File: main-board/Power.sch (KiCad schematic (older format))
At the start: 63 parts, among them J4 5V Input, Q1 N Channel, Q10 N Channel, Q11 N Channel, Q12 N Channel, Q13 P Channel, Q14 P Channel, Q15 P Channel, Q16 P Channel, Q17 P Channel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

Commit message: Swap power filter caps, tighten up trace routing
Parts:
- C47: footprint Capacitors_SMD:CP_Elec_5x4.5 -> Capacitors_SMD:CP_Elec_4x4.5
- C48: footprint Capacitors_SMD:CP_Elec_4x4.5 -> Capacitors_SMD:CP_Elec_5x5.3
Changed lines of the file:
@@
 F 0 "C47" H 1341 1596 50  0000 L CNN
 F 1 "10uF" H 1341 1505 50  0000 L CNN
-F 2 "Capacitors_SMD:CP_Elec_5x4.5" H 1250 1550 50  0001 C CNN
+F 2 "Capacitors_SMD:CP_Elec_4x4.5" H 1250 1550 50  0001 C CNN
 F 3 "~" H 1250 1550 50  0001 C CNN
 	1    1250 1550
@@
 F 0 "C48" H 2391 1596 50  0000 L CNN
 F 1 "22uF" H 2391 1505 50  0000 L CNN
-F 2 "Capacitors_SMD:CP_Elec_4x4.5" H 2300 1550 50  0001 C CNN
+F 2 "Capacitors_SMD:CP_Elec_5x5.3" H 2300 1550 50  0001 C CNN
 F 3 "~" H 2300 1550 50  0001 C CNN
 	1    2300 1550

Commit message: GPIO control lines for the MOSFET array
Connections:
- net PWR1_Control renamed PWR1_CTRL
- net PWR2_Control renamed PWR2_CTRL
- net PWR3_Control renamed PWR3_CTRL
- net PWR4_Control renamed PWR4_CTRL
- net PWR5_Control renamed PWR5_CTRL
- net PWR6_Control renamed PWR6_CTRL
- net PWR7_Control renamed PWR7_CTRL
- net PWR8_Control renamed PWR8_CTRL
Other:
- moved on the sheet: C54, C55, C56, C57, FB10, FB12, FB14, FB16, Q10, Q11, Q12, Q13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

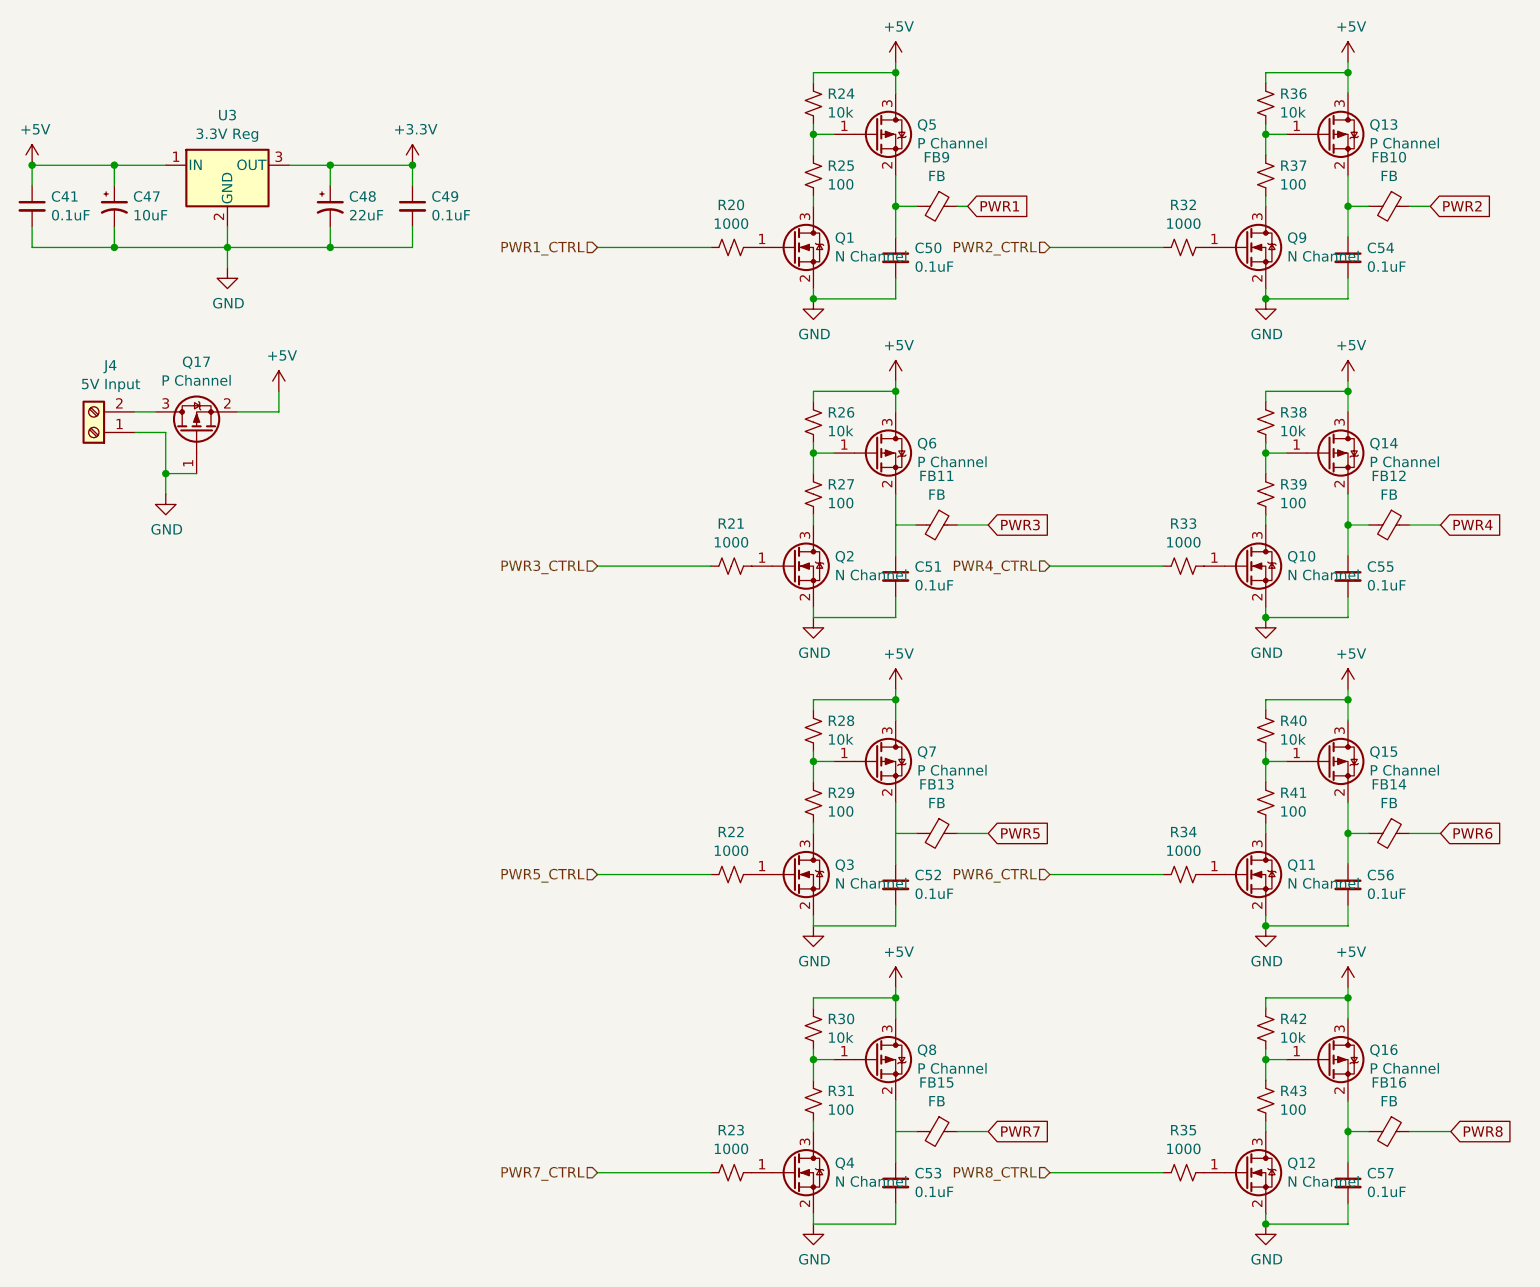
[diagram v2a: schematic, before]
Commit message: Had the p-channel FETs in the wrong orientation, and an unnecessary resistor.
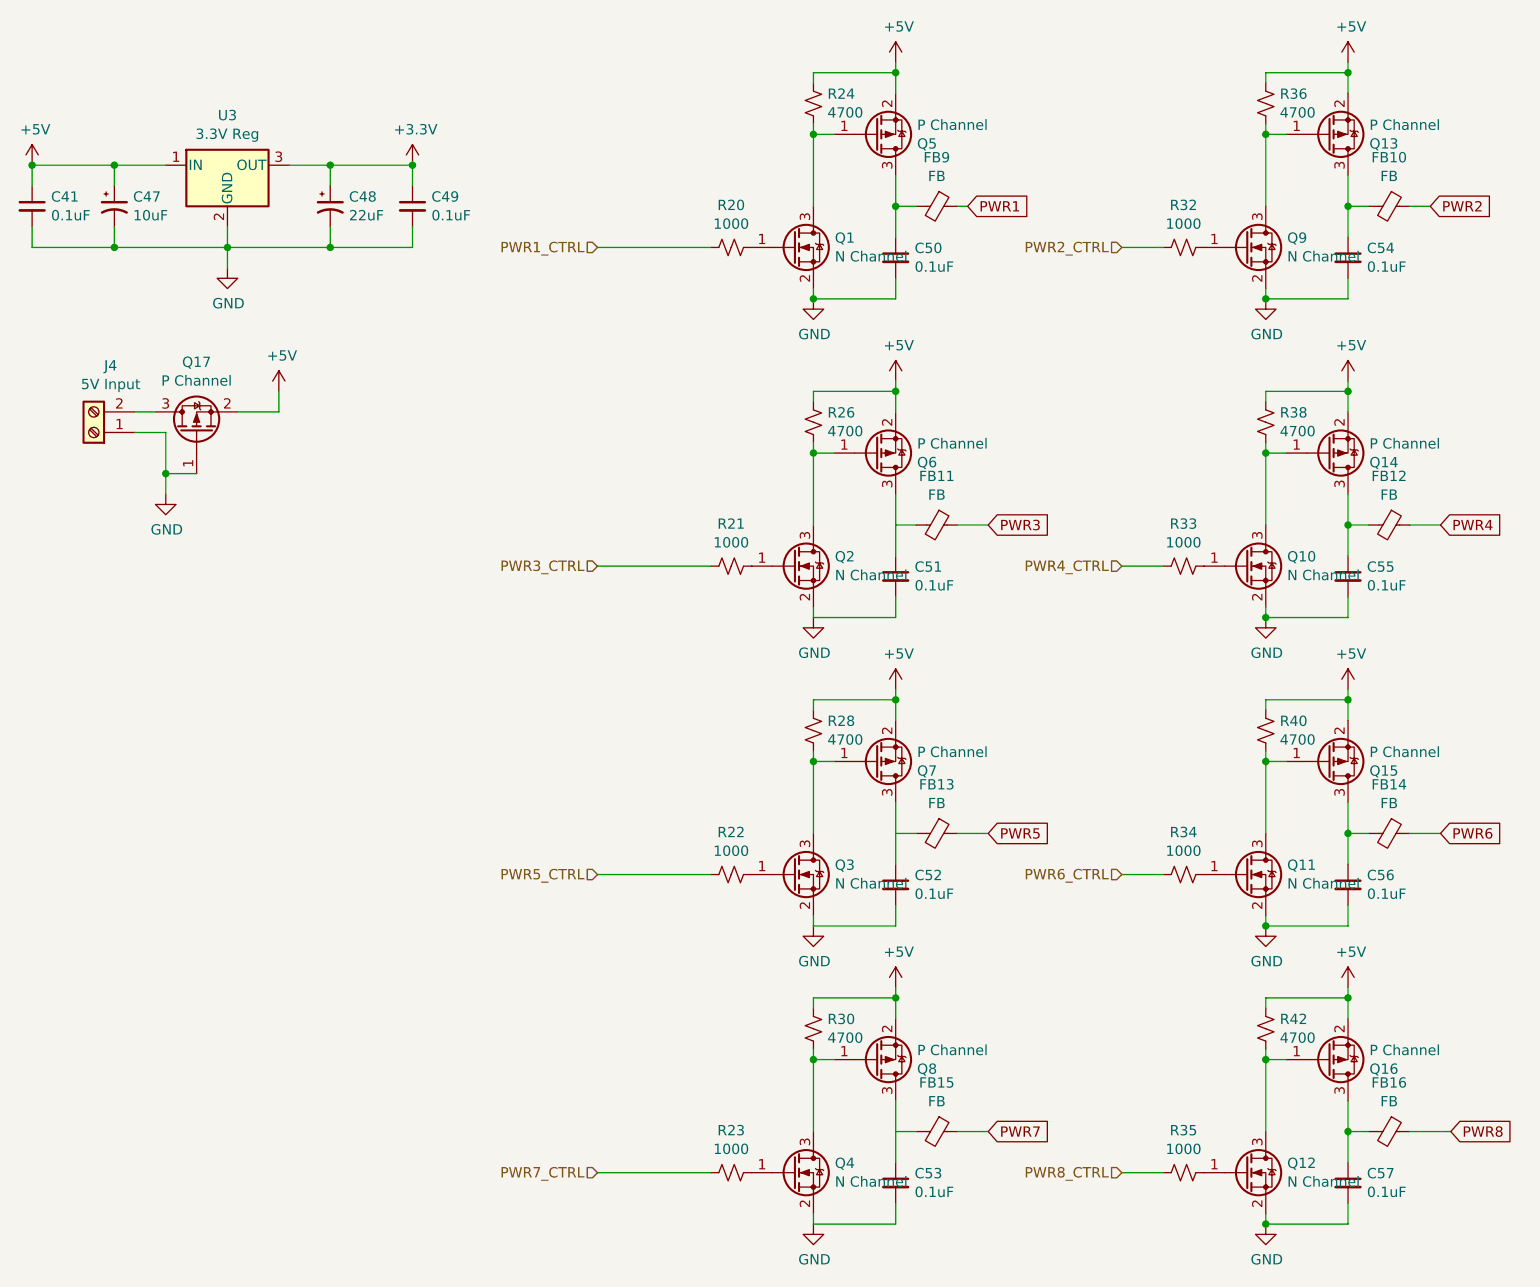
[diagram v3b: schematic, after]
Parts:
- removed R25, R27, R29, R31, R37, R39, R41, R43: 100, Resistors_SMD:R_0805, symbol Device:R_Small_US
- R24, R26, R28, R30, R36, R38, R40, R42: value 10k -> 4700
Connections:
- net +5V: now also Q13.2 (S), Q14.2 (S), Q15.2 (S), Q16.2 (S), Q5.2 (S), Q6.2 (S), Q7.2 (S), Q8.2 (S); no longer Q13.3 (D), Q14.3 (D), Q15.3 (D), Q16.3 (D), Q5.3 (D), Q6.3 (D), Q7.3 (D), Q8.3 (D)
- net at C50.1, FB9.2: now also Q5.3 (D); no longer Q5.2 (S)
- net at C57.1, FB16.2: now also Q16.3 (D); no longer Q16.2 (S)
- net at C53.1, FB15.2: now also Q8.3 (D); no longer Q8.2 (S)
- net at C52.1, FB13.2: now also Q7.3 (D); no longer Q7.2 (S)
- net at C56.1, FB14.2: now also Q15.3 (D); no longer Q15.2 (S)
- net at C51.1, FB11.2: now also Q6.3 (D); no longer Q6.2 (S)
- net at C55.1, FB12.2: now also Q14.3 (D); no longer Q14.2 (S)
- net at C54.1, FB10.2: now also Q13.3 (D); no longer Q13.2 (S)
- net at Q5.1 (G), R24.2: now also Q1.3 (D)
- net at Q13.1 (G), R36.2: now also Q9.3 (D)
- net at Q6.1 (G), R26.2: now also Q2.3 (D)
- net at Q14.1 (G), R38.2: now also Q10.3 (D)
- net at Q7.1 (G), R28.2: now also Q3.3 (D)
- net at Q15.1 (G), R40.2: now also Q11.3 (D)
- net at Q8.1 (G), R30.2: now also Q4.3 (D)
- net at Q16.1 (G), R42.2: now also Q12.3 (D)
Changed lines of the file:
@@
 P 4650 1050
 F 0 "R24" H 4718 1096 50  0000 L CNN
-F 1 "10k" H 4718 1005 50  0000 L CNN
+F 1 "4700" H 4718 1005 50  0000 L CNN
 F 2 "Resistors_SMD:R_0805" H 4650 1050 50  0001 C CNN
 F 3 "~" H 4650 1050 50  0001 C CNN
@@
 	4650 1200 4750 1200
 Connection ~ 4650 1200
-Wire Wire Line
-	4650 1300 4650 1200
-$Comp
-L Device:R_Small_US R25
-U 1 1 611CCFA1
-P 4650 1400
-F 0 "R25" H 4718 1446 50  0000 L CNN
-F 1 "100" H 4718 1355 50  0000 L CNN
-F 2 "Resistors_SMD:R_0805" H 4650 1400 50  0001 C CNN
-F 3 "~" H 4650 1400 50  0001 C CNN
-	1    4650 1400
-	1    0    0    -1
-$EndComp
-Wire Wire Line
-	4650 1550 4650 1500
 Wire Wire Line
 	4650 1950 4650 2000
@@
 F 3 "~" H 4950 1200 50  0001 C CNN
 	1    4950 1200
-	1    0    0    -1
+	1    0    0    1
 $EndComp
 $Comp
@@
 P 6850 1050
 F 0 "R36" H 6918 1096 50  0000 L CNN
-F 1 "10k" H 6918 1005 50  0000 L CNN
+F 1 "4700" H 6918 1005 50  0000 L CNN
 F 2 "Resistors_SMD:R_0805" H 6850 1050 50  0001 C CNN
 F 3 "~" H 6850 1050 50  0001 C CNN
@@
 	6850 1200 6950 1200
 Connection ~ 6850 1200
-Wire Wire Line
-	6850 1300 6850 1200
-$Comp
-L Device:R_Small_US R37
-U 1 1 611DCBB1
-P 6850 1400
-F 0 "R37" H 6918 1446 50  0000 L CNN
-F 1 "100" H 6918 1355 50  0000 L CNN
-F 2 "Resistors_SMD:R_0805" H 6850 1400 50  0001 C CNN
-F 3 "~" H 6850 1400 50  0001 C CNN
-	1    6850 1400
-	1    0    0    -1
-$EndComp
-Wire Wire Line
-	6850 1550 6850 1500
 Wire Wire Line
 	6850 1950 6850 2000
@@
 $EndComp
 Wire Wire Line
-	6350 1750 5800 1750
+	6350 1750 6150 1750
 $Comp
 L Device:Q_NMOS_GSD Q9
@@
 F 3 "~" H 7150 1200 50  0001 C CNN
 	1    7150 1200
-	1    0    0    -1
+	1    0    0    1
 $EndComp
 $Comp
@@
 P 4650 2600
 F 0 "R26" H 4718 2646 50  0000 L CNN
-F 1 "10k" H 4718 2555 50  0000 L CNN
+F 1 "4700" H 4718 2555 50  0000 L CNN
 F 2 "Resistors_SMD:R_0805" H 4650 2600 50  0001 C CNN
 F 3 "~" H 4650 2600 50  0001 C CNN
@@
 	4650 2750 4750 2750
 Connection ~ 4650 2750
-Wire Wire Line
-	4650 2850 4650 2750
-$Comp
-L Device:R_Small_US R27
-U 1 1 611F4F2B
-P 4650 2950
-F 0 "R27" H 4718 2996 50  0000 L CNN
-F 1 "100" H 4718 2905 50  0000 L CNN
-F 2 "Resistors_SMD:R_0805" H 4650 2950 50  0001 C CNN
-F 3 "~" H 4650 2950 50  0001 C CNN
-	1    4650 2950
-	1    0    0    -1
-$EndComp
-Wire Wire Line
-	4650 3100 4650 3050
 Wire Wire Line
 	4650 3500 4650 3550
@@
 F 3 "~" H 4950 2750 50  0001 C CNN
 	1    4950 2750
-	1    0    0    -1
+	1    0    0    1
 $EndComp
 $Comp
@@
 P 6850 2600
 F 0 "R38" H 6918 2646 50  0000 L CNN
-F 1 "10k" H 6918 2555 50  0000 L CNN
+F 1 "4700" H 6918 2555 50  0000 L CNN
 F 2 "Resistors_SMD:R_0805" H 6850 2600 50  0001 C CNN
 F 3 "~" H 6850 2600 50  0001 C CNN
@@
 	6850 2750 6950 2750
 Connection ~ 6850 2750
-Wire Wire Line
-	6850 2850 6850 2750
-$Comp
-L Device:R_Small_US R39
-U 1 1 611F4F65
-P 6850 2950
-F 0 "R39" H 6918 2996 50  0000 L CNN
-F 1 "100" H 6918 2905 50  0000 L CNN
-F 2 "Resistors_SMD:R_0805" H 6850 2950 50  0001 C CNN
-F 3 "~" H 6850 2950 50  0001 C CNN
-	1    6850 2950
-	1    0    0    -1
-$EndComp
-Wire Wire Line
-	6850 3100 6850 3050
 Wire Wire Line
 	6850 3500 6850 3550
@@
 $EndComp
 Wire Wire Line
-	6350 3300 5800 3300
+	6350 3300 6150 3300
 $Comp
 L Device:Q_NMOS_GSD Q10
@@
 F 3 "~" H 7150 2750 50  0001 C CNN
 	1    7150 2750
-	1    0    0    -1
+	1    0    0    1
 $EndComp
 $Comp
@@
 P 4650 4100
 F 0 "R28" H 4718 4146 50  0000 L CNN
-F 1 "10k" H 4718 4055 50  0000 L CNN
+F 1 "4700" H 4718 4055 50  0000 L CNN
 F 2 "Resistors_SMD:R_0805" H 4650 4100 50  0001 C CNN
 F 3 "~" H 4650 4100 50  0001 C CNN
@@
 	4650 4250 4750 4250
 Connection ~ 4650 4250
-Wire Wire Line
-	4650 4350 4650 4250
-$Comp
-L Device:R_Small_US R29
-U 1 1 611FB5A8
-P 4650 4450
-F 0 "R29" H 4718 4496 50  0000 L CNN
-F 1 "100" H 4718 4405 50  0000 L CNN
-F 2 "Resistors_SMD:R_0805" H 4650 4450 50  0001 C CNN
-F 3 "~" H 4650 4450 50  0001 C CNN
-	1    4650 4450
-	1    0    0    -1
-$EndComp
-Wire Wire Line
-	4650 4600 4650 4550
 Wire Wire Line
 	4650 5000 4650 5050
@@
 F 3 "~" H 4950 4250 50  0001 C CNN
 	1    4950 4250
-	1    0    0    -1
+	1    0    0    1
 $EndComp
 $Comp
@@
 P 6850 4100
 F 0 "R40" H 6918 4146 50  0000 L CNN
-F 1 "10k" H 6918 4055 50  0000 L CNN
+F 1 "4700" H 6918 4055 50  0000 L CNN
 F 2 "Resistors_SMD:R_0805" H 6850 4100 50  0001 C CNN
 F 3 "~" H 6850 4100 50  0001 C CNN
@@
 	6850 4250 6950 4250
 Connection ~ 6850 4250
-Wire Wire Line
-	6850 4350 6850 4250
-$Comp
-L Device:R_Small_US R41
-U 1 1 611FB5E2
-P 6850 4450
-F 0 "R41" H 6918 4496 50  0000 L CNN
-F 1 "100" H 6918 4405 50  0000 L CNN
-F 2 "Resistors_SMD:R_0805" H 6850 4450 50  0001 C CNN
-F 3 "~" H 6850 4450 50  0001 C CNN
-	1    6850 4450
-	1    0    0    -1
-$EndComp
-Wire Wire Line
-	6850 4600 6850 4550
 Wire Wire Line
 	6850 5000 6850 5050
@@
 $EndComp
 Wire Wire Line
-	6350 4800 5800 4800
+	6350 4800 6150 4800
 $Comp
 L Device:Q_NMOS_GSD Q11
@@
 F 3 "~" H 7150 4250 50  0001 C CNN
 	1    7150 4250
-	1    0    0    -1
+	1    0    0    1
 $EndComp
 $Comp
@@
 P 4650 5550
 F 0 "R30" H 4718 5596 50  0000 L CNN
-F 1 "10k" H 4718 5505 50  0000 L CNN
+F 1 "4700" H 4718 5505 50  0000 L CNN
 F 2 "Resistors_SMD:R_0805" H 4650 5550 50  0001 C CNN
 F 3 "~" H 4650 5550 50  0001 C CNN
@@
 	4650 5700 4750 5700
 Connection ~ 4650 5700
-Wire Wire Line
-	4650 5800 4650 5700
-$Comp
-L Device:R_Small_US R31
-U 1 1 6120342D
-P 4650 5900
-F 0 "R31" H 4718 5946 50  0000 L CNN
-F 1 "100" H 4718 5855 50  0000 L CNN
-F 2 "Resistors_SMD:R_0805" H 4650 5900 50  0001 C CNN
-F 3 "~" H 4650 5900 50  0001 C CNN
-	1    4650 5900
-	1    0    0    -1
-$EndComp
-Wire Wire Line
-	4650 6050 4650 6000
 Wire Wire Line
 	4650 6450 4650 6500
@@
 F 3 "~" H 4950 5700 50  0001 C CNN
 	1    4950 5700
-	1    0    0    -1
+	1    0    0    1
 $EndComp
 $Comp
@@
 P 6850 5550
 F 0 "R42" H 6918 5596 50  0000 L CNN
-F 1 "10k" H 6918 5505 50  0000 L CNN
+F 1 "4700" H 6918 5505 50  0000 L CNN
 F 2 "Resistors_SMD:R_0805" H 6850 5550 50  0001 C CNN
 F 3 "~" H 6850 5550 50  0001 C CNN
@@
 	6850 5700 6950 5700
 Connection ~ 6850 5700
-Wire Wire Line
-	6850 5800 6850 5700
-$Comp
-L Device:R_Small_US R43
-U 1 1 61203467
-P 6850 5900
-F 0 "R43" H 6918 5946 50  0000 L CNN
-F 1 "100" H 6918 5855 50  0000 L CNN
-F 2 "Resistors_SMD:R_0805" H 6850 5900 50  0001 C CNN
-F 3 "~" H 6850 5900 50  0001 C CNN
-	1    6850 5900
-	1    0    0    -1
-$EndComp
-Wire Wire Line
-	6850 6050 6850 6000
 Wire Wire Line
 	6850 6450 6850 6500
@@
 $EndComp
 Wire Wire Line
-	6350 6250 5800 6250
+	6350 6250 6150 6250
 $Comp
 L Device:Q_NMOS_GSD Q12
@@
 F 3 "~" H 7150 5700 50  0001 C CNN
 	1    7150 5700
-	1    0    0    -1
+	1    0    0    1
 $EndComp
 $Comp
@@
 Text HLabel 3600 3300 0    50   Input ~ 0
 PWR3_CTRL
-Text HLabel 5800 1750 0    50   Input ~ 0
+Text HLabel 6150 1750 0    50   Input ~ 0
 PWR2_CTRL
-Text HLabel 5800 3300 0    50   Input ~ 0
+Text HLabel 6150 3300 0    50   Input ~ 0
 PWR4_CTRL
-Text HLabel 5800 4800 0    50   Input ~ 0
+Text HLabel 6150 4800 0    50   Input ~ 0
 PWR6_CTRL
 Text HLabel 3600 4800 0    50   Input ~ 0
@@
 Text HLabel 3600 6250 0    50   Input ~ 0
 PWR7_CTRL
-Text HLabel 5800 6250 0    50   Input ~ 0
+Text HLabel 6150 6250 0    50   Input ~ 0
 PWR8_CTRL
 Connection ~ 6850 2000
@@
 Connection ~ 7250 4600
 Connection ~ 7250 6050
+Wire Wire Line
+	4650 1200 4650 1550
+Wire Wire Line
+	6850 1200 6850 1550
+Wire Wire Line
+	6850 2750 6850 3100
+Wire Wire Line
+	4650 2750 4650 3100
+Wire Wire Line
+	4650 4250 4650 4600
+Wire Wire Line
+	6850 4250 6850 4600
+Wire Wire Line
+	6850 5700 6850 6050
+Wire Wire Line
+	4650 5700 4650 6050
 $EndSCHEMATC
